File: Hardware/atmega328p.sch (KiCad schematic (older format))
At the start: 22 parts, among them J401 USART, Q101 BCV27, U401 ATMEGA328P-PU, Y401 16MHz

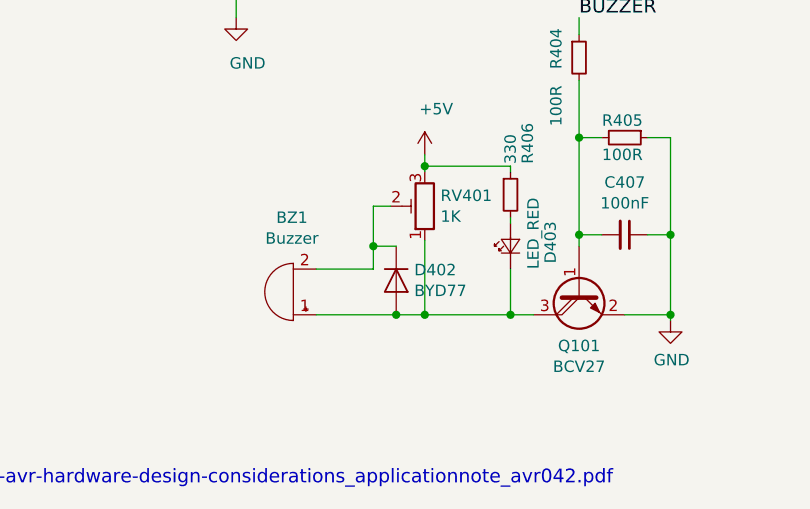
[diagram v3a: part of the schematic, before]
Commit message: 06/08/2019
Adicionei um jumper no buzzer para que ele possa ser desativado durante os testes;
separei os componentes que irão para cara conector KRE para depois serem montados
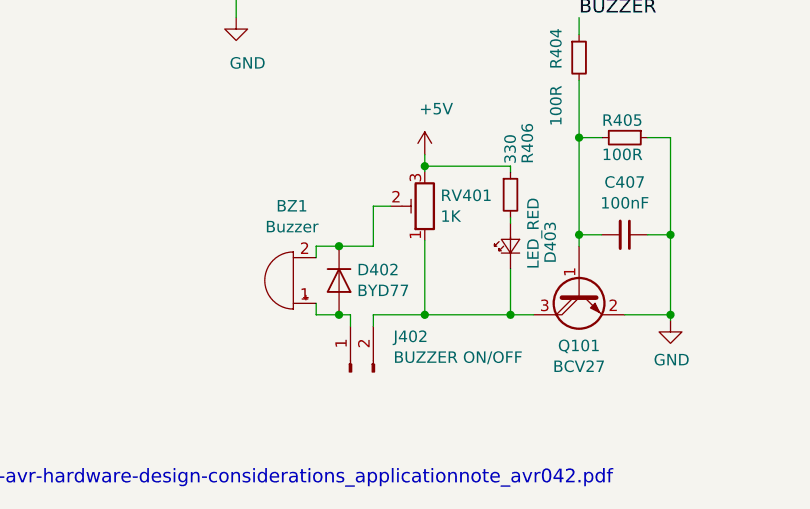
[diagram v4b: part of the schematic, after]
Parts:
- added J402: BUZZER ON/OFF, Connector_PinHeader_2.54mm:PinHeader_1x02_P2.54mm_Vertical, symbol Connector:Conn_01x02_Male
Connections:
- net at D403.1 (K), Q101.3 (C), RV401.1: now also J402.2 (Pin_2); no longer BZ1.1 (-), D402.2 (A)
- new net: BZ1.1 (-), D402.2 (A), J402.1 (Pin_1)
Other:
- moved on the sheet: BZ1, D402
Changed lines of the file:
@@
 L Device:Buzzer BZ1
 U 1 1 5CCB1F93
-P 4600 6850
-F 0 "BZ1" H 4606 6525 50  0000 C CNN
-F 1 "Buzzer" H 4606 6616 50  0000 C CNN
-F 2 "Buzzer_Beeper:Buzzer_12x9.5RM7.6" V 4575 6950 50  0001 C CNN
-F 3 "~" V 4575 6950 50  0001 C CNN
-	1    4600 6850
+P 4600 6800
+F 0 "BZ1" H 4606 6475 50  0000 C CNN
+F 1 "Buzzer" H 4606 6566 50  0000 C CNN
+F 2 "Buzzer_Beeper:Buzzer_12x9.5RM7.6" V 4575 6900 50  0001 C CNN
+F 3 "~" V 4575 6900 50  0001 C CNN
+	1    4600 6800
 	-1   0    0    1
-$EndComp
-$Comp
-L Device:D D402
-U 1 1 5CCB20DF
-P 5050 6800
-F 0 "D402" V 5004 6879 50  0000 L CNN
-F 1 "BYD77" V 5095 6879 50  0000 L CNN
-F 2 "Diode_SMD:D_MiniMELF_Handsoldering" H 5050 6800 50  0001 C CNN
-F 3 "~" H 5050 6800 50  0001 C CNN
-	1    5050 6800
-	0    1    1    0
 $EndComp
 Wire Wire Line
@@
 	5175 6300 5175 6325
 Wire Wire Line
-	4700 6950 5050 6950
-Wire Wire Line
-	4700 6750 4950 6750
-Wire Wire Line
-	4950 6750 4950 6650
-Wire Wire Line
 	4950 6475 5025 6475
-Connection ~ 5050 6950
-Wire Wire Line
-	5050 6650 4950 6650
-Connection ~ 4950 6650
 Wire Wire Line
 	4950 6650 4950 6475
 Wire Wire Line
 	5175 6625 5175 6950
-Wire Wire Line
-	5050 6950 5175 6950
-Connection ~ 5175 6950
 Wire Wire Line
 	5175 6950 5550 6950
@@
 Wire Wire Line
 	4350 1850 4350 2350
+$Comp
+L Connector:Conn_01x02_Male J402
+U 1 1 5D49F57B
+P 4850 7200
+F 0 "J402" V 5004 7012 50  0000 R CNN
+F 1 "BUZZER ON/OFF" V 4913 7012 50  0000 R CNN
+F 2 "Connector_PinHeader_2.54mm:PinHeader_1x02_P2.54mm_Vertical" H 4850 7200 50  0001 C CNN
+F 3 "~" H 4850 7200 50  0001 C CNN
+	1    4850 7200
+	0    -1   -1   0
+$EndComp
+Wire Wire Line
+	4800 6950 4700 6950
+Wire Wire Line
+	4700 6950 4700 6900
+Wire Wire Line
+	4700 6700 4700 6650
+Wire Wire Line
+	4700 6650 4800 6650
+Wire Wire Line
+	4950 6650 4800 6650
+Connection ~ 4800 6650
+$Comp
+L Device:D D402
+U 1 1 5CCB20DF
+P 4800 6800
+F 0 "D402" V 4754 6879 50  0000 L CNN
+F 1 "BYD77" V 4845 6879 50  0000 L CNN
+F 2 "Diode_SMD:D_MiniMELF_Handsoldering" H 4800 6800 50  0001 C CNN
+F 3 "~" H 4800 6800 50  0001 C CNN
+	1    4800 6800
+	0    1    1    0
+$EndComp
+Wire Wire Line
+	4800 6950 4850 6950
+Wire Wire Line
+	4850 6950 4850 7000
+Connection ~ 4800 6950
+Wire Wire Line
+	4950 7000 4950 6950
+Wire Wire Line
+	4950 6950 5175 6950
+Connection ~ 5175 6950
 $EndSCHEMATC

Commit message: Modelo final
Terminado os conectores e a topologia
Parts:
- removed J402: BUZZER ON/OFF, Connector_PinHeader_2.54mm:PinHeader_1x02_P2.54mm_Vertical, symbol Connector:Conn_01x02_Male
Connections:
- net at D403.1 (K), Q101.3 (C), RV401.1: now also BZ1.1 (-), D402.2 (A)
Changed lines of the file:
@@
 EESchema Schematic File Version 4
 LIBS:MIC19-cache
-EELAYER 29 0
+EELAYER 26 0
 EELAYER END
 $Descr A4 11693 8268
@@
 Wire Wire Line
 	4350 1850 4350 2350
-$Comp
-L Connector:Conn_01x02_Male J402
-U 1 1 5D49F57B
-P 4850 7200
-F 0 "J402" V 5004 7012 50  0000 R CNN
-F 1 "BUZZER ON/OFF" V 4913 7012 50  0000 R CNN
-F 2 "Connector_PinHeader_2.54mm:PinHeader_1x02_P2.54mm_Vertical" H 4850 7200 50  0001 C CNN
-F 3 "~" H 4850 7200 50  0001 C CNN
-	1    4850 7200
-	0    -1   -1   0
-$EndComp
 Wire Wire Line
 	4800 6950 4700 6950
@@
 	0    1    1    0
 $EndComp
-Wire Wire Line
-	4800 6950 4850 6950
-Wire Wire Line
-	4850 6950 4850 7000
 Connection ~ 4800 6950
-Wire Wire Line
-	4950 7000 4950 6950
-Wire Wire Line
-	4950 6950 5175 6950
 Connection ~ 5175 6950
+Wire Wire Line
+	4800 6950 5175 6950
 $EndSCHEMATC

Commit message: Buzzer estava invertido, alimentações melhoradas. A alimentação do atmega foi isolada em relação aos switches.
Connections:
- net +5V: now also RV401.1; no longer RV401.3
- net at D402.2 (A), D403.1 (K), Q101.3 (C): now also BZ1.2 (+), RV401.3; no longer BZ1.1 (-), RV401.1
- net at D402.1 (K), RV401.2: now also BZ1.1 (-); no longer BZ1.2 (+)
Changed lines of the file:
@@
 EESchema Schematic File Version 4
 LIBS:MIC19-cache
-EELAYER 26 0
+EELAYER 29 0
 EELAYER END
 $Descr A4 11693 8268
@@
 	0    -1   1    0
 $EndComp
-$Comp
-L Device:Buzzer BZ1
-U 1 1 5CCB1F93
-P 4600 6800
-F 0 "BZ1" H 4606 6475 50  0000 C CNN
-F 1 "Buzzer" H 4606 6566 50  0000 C CNN
-F 2 "Buzzer_Beeper:Buzzer_12x9.5RM7.6" V 4575 6900 50  0001 C CNN
-F 3 "~" V 4575 6900 50  0001 C CNN
-	1    4600 6800
-	-1   0    0    1
-$EndComp
 Wire Wire Line
 	4350 5350 4350 5450
@@
 F 3 "~" H 5175 6475 50  0001 C CNN
 	1    5175 6475
-	-1   0    0    1
+	-1   0    0    -1
 $EndComp
 Wire Wire Line
@@
 Wire Wire Line
 	4800 6950 5175 6950
+$Comp
+L Device:Buzzer BZ1
+U 1 1 5CCB1F93
+P 4600 6800
+F 0 "BZ1" H 4606 6475 50  0000 C CNN
+F 1 "Buzzer" H 4606 6566 50  0000 C CNN
+F 2 "Buzzer_Beeper:Buzzer_12x9.5RM7.6" V 4575 6900 50  0001 C CNN
+F 3 "~" V 4575 6900 50  0001 C CNN
+	1    4600 6800
+	-1   0    0    -1
+$EndComp
 $EndSCHEMATC

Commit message: Conferido e Finalizado
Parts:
- removed C405: 100nF, Capacitor_SMD:C_0805_2012Metric_Pad1.15x1.40mm_HandSolder, symbol Device:C_Small
- added R407: 100R, Resistor_SMD:R_0805_2012Metric_Pad1.15x1.40mm_HandSolder, symbol Device:R_Small
- C406: value 100nF -> 10nF
- R402, R403: value 1k -> 100R
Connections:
- net RESET: now also J401.4 (Pin_4), R407.2; no longer U401.1 (~RESET~/PC6)
- new net: R407.1, U401.1 (~RESET~/PC6)
- no-connect marks 1 -> 2
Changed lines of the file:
@@
 EESchema Schematic File Version 4
 LIBS:MIC19-cache
-EELAYER 29 0
+EELAYER 30 0
 EELAYER END
 $Descr A4 11693 8268
@@
 P 6150 4350
 F 0 "C406" V 6050 4250 50  0000 L CNN
-F 1 "100nF" V 6200 4400 50  0000 L CNN
+F 1 "10nF" V 6200 4400 50  0000 L CNN
 F 2 "Capacitor_SMD:C_0805_2012Metric_Pad1.15x1.40mm_HandSolder" H 6150 4350 50  0001 C CNN
 F 3 "" H 6150 4350 50  0001 C CNN
@@
 P 7350 4350
 F 0 "R402" V 7400 4450 50  0000 L CNN
-F 1 "1k" V 7400 4200 50  0000 L CNN
+F 1 "100R" V 7400 4200 50  0000 L CNN
 F 2 "Resistor_SMD:R_0805_2012Metric_Pad1.15x1.40mm_HandSolder" H 7350 4350 50  0001 C CNN
 F 3 "" H 7350 4350 50  0001 C CNN
@@
 P 7350 4450
 F 0 "R403" V 7400 4550 50  0000 L CNN
-F 1 "1k" V 7400 4300 50  0000 L CNN
+F 1 "100R" V 7400 4300 50  0000 L CNN
 F 2 "Resistor_SMD:R_0805_2012Metric_Pad1.15x1.40mm_HandSolder" H 7350 4450 50  0001 C CNN
 F 3 "" H 7350 4450 50  0001 C CNN
@@
 	5975 3750 5975 3850
 Connection ~ 5975 3850
-$Comp
-L Device:C_Small C405
-U 1 1 5BED8033
-P 6525 4250
-F 0 "C405" V 6625 4100 50  0000 L CNN
-F 1 "100nF" V 6625 3850 50  0000 L CNN
-F 2 "Capacitor_SMD:C_0805_2012Metric_Pad1.15x1.40mm_HandSolder" H 6525 4250 50  0001 C CNN
-F 3 "" H 6525 4250 50  0001 C CNN
-	1    6525 4250
-	0    -1   -1   0
-$EndComp
 Text Label 5050 4450 0    60   ~ 0
 USART_RX
-Wire Wire Line
-	6625 4250 7550 4250
 $Comp
 L power:GND #PWR0409
@@
 SW_PUMP3_ON
 Wire Wire Line
-	6300 4250 6425 4250
-Wire Wire Line
 	5975 4200 5975 4250
 Wire Wire Line
-	4950 4250 5975 4250
+	4950 4250 5425 4250
 Wire Wire Line
 	5975 4400 5975 4350
@@
 	-1   0    0    -1
 $EndComp
+Wire Wire Line
+	6300 4250 7550 4250
+$Comp
+L Device:R_Small R407
+U 1 1 5D5DE1E3
+P 5525 4250
+F 0 "R407" V 5575 4350 50  0000 L CNN
+F 1 "100R" V 5575 4100 50  0000 L CNN
+F 2 "Resistor_SMD:R_0805_2012Metric_Pad1.15x1.40mm_HandSolder" H 5525 4250 50  0001 C CNN
+F 3 "" H 5525 4250 50  0001 C CNN
+	1    5525 4250
+	0    -1   -1   0
+$EndComp
+Wire Wire Line
+	5625 4250 5975 4250
+NoConn ~ 15050 4450
 $EndSCHEMATC
